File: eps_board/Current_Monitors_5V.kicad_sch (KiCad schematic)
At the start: 6 parts, among them U52 TCAL9538, U53 TCAL9538

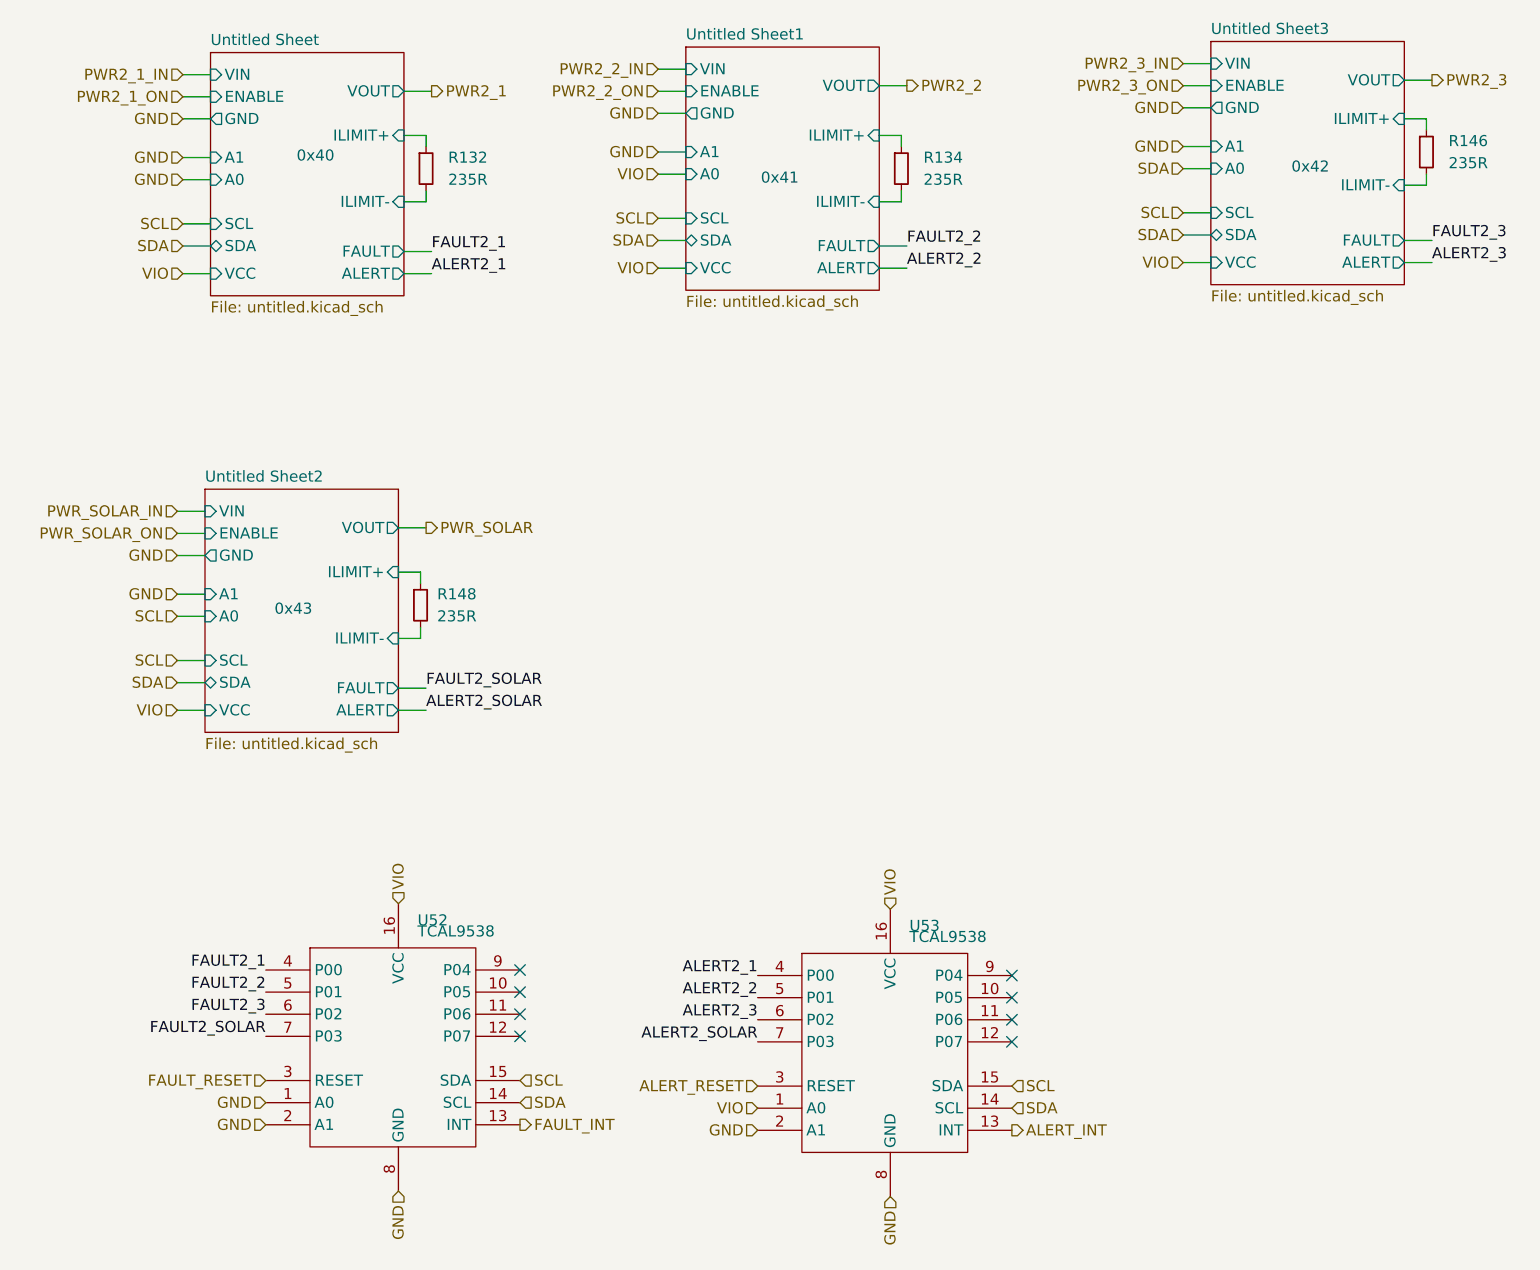
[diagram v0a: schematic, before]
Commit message: combine interrupts per powerline and use i2c expanders to turn on and solicit feedback
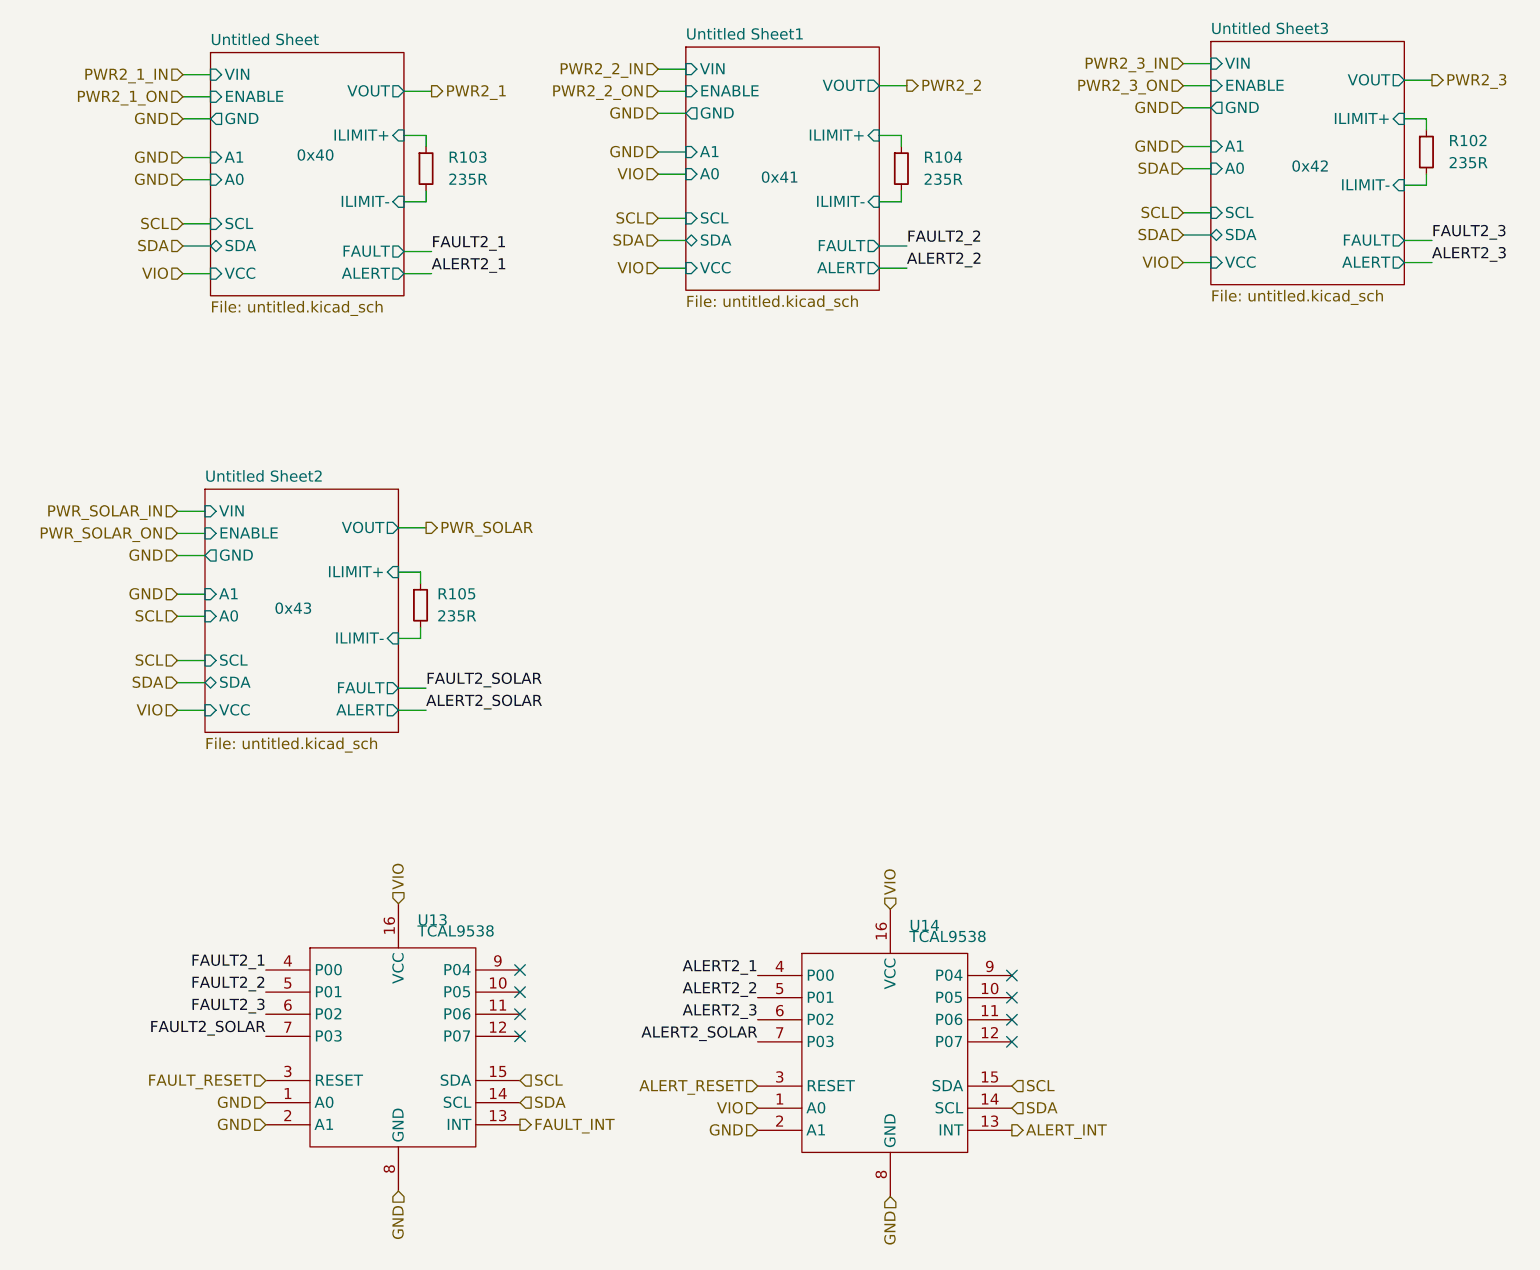
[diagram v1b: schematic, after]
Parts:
- renumbered R146 to R102, R132 to R103, R134 to R104, R148 to R105, U52 to U13, U53 to U14
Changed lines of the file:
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@@
 		(dnp no)
 		(fields_autoplaced yes)
-		(property "Reference" "U52"
+		(property "Reference" "U13"
 			(at 62.5191 128.27 0)
 			(effects
@@
 		)
 		(instances
-			(project ""
-				(path "/05170af6-30ef-4c3a-b972-f098085da1bc/7ff60e90-d7e1-4395-9fc2-090dd6f49528"
-					(reference "U52")
+			(project "EPS"
+				(path "/05170af6-30ef-4c3a-b972-f098085da1bc/f49efc77-2d97-4e89-878d-4d3bf2059c2a"
+					(reference "U13")
 					(unit 1)
 				)
@@
 		(dnp no)
 		(fields_autoplaced yes)
-		(property "Reference" "U53"
+		(property "Reference" "U14"
 			(at 119.0341 128.905 0)
 			(effects
@@
 		(instances
 			(project "EPS"
-				(path "/05170af6-30ef-4c3a-b972-f098085da1bc/7ff60e90-d7e1-4395-9fc2-090dd6f49528"
-					(reference "U53")
+				(path "/05170af6-30ef-4c3a-b972-f098085da1bc/f49efc77-2d97-4e89-878d-4d3bf2059c2a"
+					(reference "U14")
 					(unit 1)
 				)
@@
 		(dnp no)
 		(fields_autoplaced yes)
-		(property "Reference" "R132"
+		(property "Reference" "R103"
 			(at 66.04 40.6399 0)
 			(effects
@@
 		)
 		(instances
-			(project ""
-				(path "/05170af6-30ef-4c3a-b972-f098085da1bc/7ff60e90-d7e1-4395-9fc2-090dd6f49528"
-					(reference "R132")
+			(project "EPS"
+				(path "/05170af6-30ef-4c3a-b972-f098085da1bc/f49efc77-2d97-4e89-878d-4d3bf2059c2a"
+					(reference "R103")
 					(unit 1)
 				)
@@
 		(dnp no)
 		(fields_autoplaced yes)
-		(property "Reference" "R146"
+		(property "Reference" "R102"
 			(at 180.975 38.7349 0)
 			(effects
@@
 		(instances
 			(project "EPS"
-				(path "/05170af6-30ef-4c3a-b972-f098085da1bc/7ff60e90-d7e1-4395-9fc2-090dd6f49528"
-					(reference "R146")
+				(path "/05170af6-30ef-4c3a-b972-f098085da1bc/f49efc77-2d97-4e89-878d-4d3bf2059c2a"
+					(reference "R102")
 					(unit 1)
 				)
@@
 		(dnp no)
 		(fields_autoplaced yes)
-		(property "Reference" "R148"
+		(property "Reference" "R105"
 			(at 64.77 90.8049 0)
 			(effects
@@
 		(instances
 			(project "EPS"
-				(path "/05170af6-30ef-4c3a-b972-f098085da1bc/7ff60e90-d7e1-4395-9fc2-090dd6f49528"
-					(reference "R148")
+				(path "/05170af6-30ef-4c3a-b972-f098085da1bc/f49efc77-2d97-4e89-878d-4d3bf2059c2a"
+					(reference "R105")
 					(unit 1)
 				)
@@
 		(dnp no)
 		(fields_autoplaced yes)
-		(property "Reference" "R134"
+		(property "Reference" "R104"
 			(at 120.65 40.6399 0)
 			(effects
@@
 		(instances
 			(project "EPS"
-				(path "/05170af6-30ef-4c3a-b972-f098085da1bc/7ff60e90-d7e1-4395-9fc2-090dd6f49528"
-					(reference "R134")
+				(path "/05170af6-30ef-4c3a-b972-f098085da1bc/f49efc77-2d97-4e89-878d-4d3bf2059c2a"
+					(reference "R104")
 					(unit 1)
 				)
@@
 		(instances
 			(project "EPS"
-				(path "/05170af6-30ef-4c3a-b972-f098085da1bc/7ff60e90-d7e1-4395-9fc2-090dd6f49528"
+				(path "/05170af6-30ef-4c3a-b972-f098085da1bc/f49efc77-2d97-4e89-878d-4d3bf2059c2a"
 					(page "44")
 				)
@@
 		(instances
 			(project "EPS"
-				(path "/05170af6-30ef-4c3a-b972-f098085da1bc/7ff60e90-d7e1-4395-9fc2-090dd6f49528"
+				(path "/05170af6-30ef-4c3a-b972-f098085da1bc/f49efc77-2d97-4e89-878d-4d3bf2059c2a"
 					(page "46")
 				)
@@
 		(instances
 			(project "EPS"
-				(path "/05170af6-30ef-4c3a-b972-f098085da1bc/7ff60e90-d7e1-4395-9fc2-090dd6f49528"
-					(page "43")
+				(path "/05170af6-30ef-4c3a-b972-f098085da1bc/f49efc77-2d97-4e89-878d-4d3bf2059c2a"
+					(page "42")
 				)
 			)
@@
 		(instances
 			(project "EPS"
-				(path "/05170af6-30ef-4c3a-b972-f098085da1bc/7ff60e90-d7e1-4395-9fc2-090dd6f49528"
-					(page "42")
-				)
-			)
+				(path "/05170af6-30ef-4c3a-b972-f098085da1bc/f49efc77-2d97-4e89-878d-4d3bf2059c2a"
+					(page "43")
+				)
+			)
